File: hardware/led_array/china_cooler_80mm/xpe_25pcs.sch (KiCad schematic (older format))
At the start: 25 parts

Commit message: initial 80mm pcb draft ready
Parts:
- removed D10, D2, D3, D4, D5, D6, D7, D8, D9: royal blue, LEDs:LED-XP-G_CREE, symbol LED
- removed D11, D12, D13, D14, D15: blue, LEDs:LED-XP-G_CREE, symbol LED
- removed D16, D17, D18, D19, D20: white, LEDs:LED-XP-G_CREE, symbol LED
- removed D21, D22, D23, D24, D25: white_warm, LEDs:LED-XP-G_CREE, symbol LED
- added D1, D10, D2, D3, D4, D6, D7, D8, D9: royal blue, led:LED_Cree-XP-E, symbol led:LED
- added D11, D12, D13, D14, D15: blue, led:LED_Cree-XP-E, symbol led:LED
- added D16, D17, D18, D19, D20: white, led:LED_Cree-XP-E, symbol led:LED
- added D21, D22, D23, D24, D25: white_warm, led:LED_Cree-XP-E, symbol led:LED
- added J1: Conn_01x10, led:header_10_smd, symbol Connector_Generic:Conn_01x10
- D5: renamed from D1; footprint LEDs:LED-XP-G_CREE -> led:LED_Cree-XP-E; symbol LED -> led:LED
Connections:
- net GND: now also D5.1 (K), D10.1 (K), D15.1 (K), D20.1 (K), D25.1 (K), J1.10 (Pin_10), J1.6 (Pin_6), J1.7 (Pin_7), J1.8 (Pin_8), J1.9 (Pin_9)
- net at D5.2 (A): now also D4.1 (K)
- new net: D10.2 (A), D9.1 (K)
- new net: D3.1 (K), D4.2 (A)
- new net: D8.1 (K), D9.2 (A)
- new net: D2.1 (K), D3.2 (A)
- new net: D7.1 (K), D8.2 (A)
- new net: D1.1 (K), D2.2 (A)
- new net: D6.1 (K), D7.2 (A)
- new net: D1.2 (A), J1.5 (Pin_5)
- new net: D6.2 (A), J1.4 (Pin_4)
- new net: D14.1 (K), D15.2 (A)
- new net: D19.1 (K), D20.2 (A)
- new net: D21.2 (A), J1.1 (Pin_1)
- new net: D16.2 (A), J1.2 (Pin_2)
- new net: D11.2 (A), J1.3 (Pin_3)
- new net: D24.1 (K), D25.2 (A)
- new net: D13.1 (K), D14.2 (A)
- new net: D18.1 (K), D19.2 (A)
- new net: D23.1 (K), D24.2 (A)
- new net: D12.1 (K), D13.2 (A)
- new net: D17.1 (K), D18.2 (A)
- new net: D22.1 (K), D23.2 (A)
- new net: D11.1 (K), D12.2 (A)
- new net: D16.1 (K), D17.2 (A)
- new net: D21.1 (K), D22.2 (A)

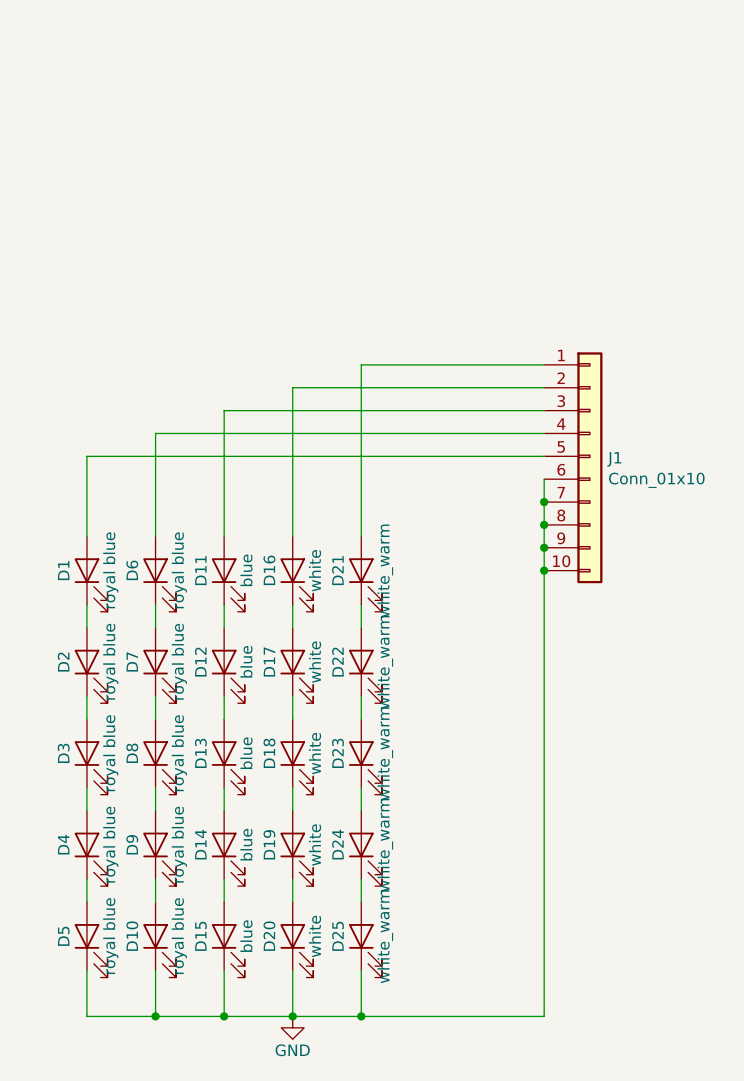
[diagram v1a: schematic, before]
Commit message: 25 led array improved
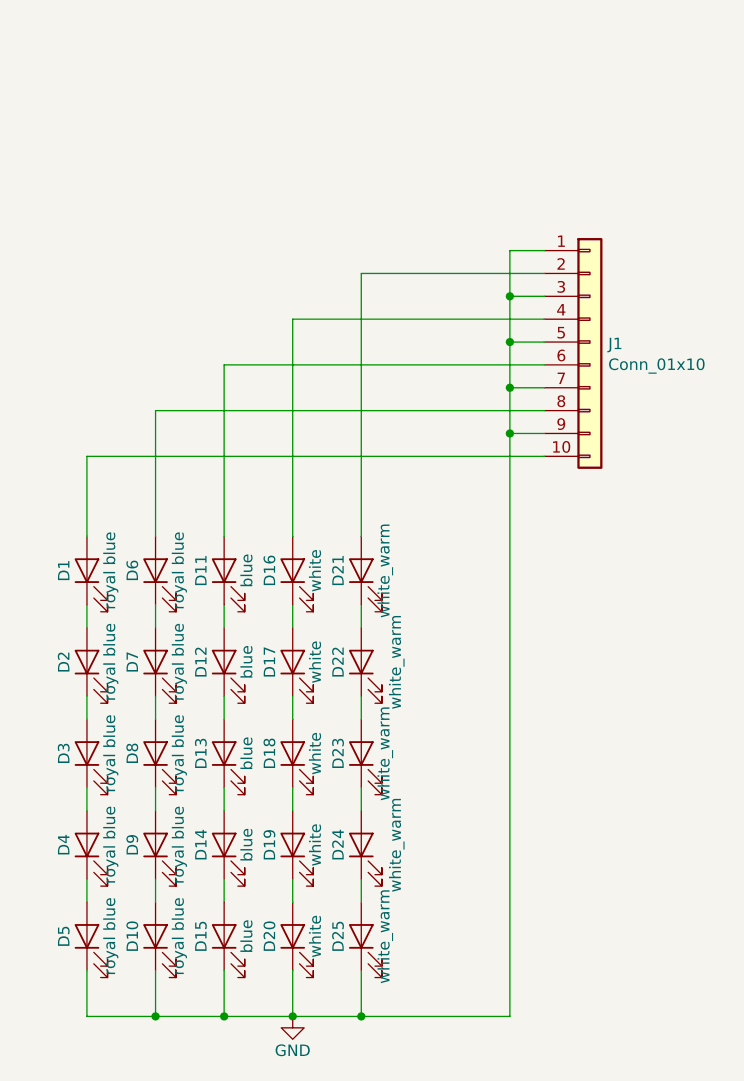
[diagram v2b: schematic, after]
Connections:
- net GND: now also J1.1 (Pin_1), J1.3 (Pin_3), J1.5 (Pin_5); no longer J1.10 (Pin_10), J1.6 (Pin_6), J1.8 (Pin_8)
- net at D1.2 (A): now also J1.10 (Pin_10); no longer J1.5 (Pin_5)
- net at D6.2 (A): now also J1.8 (Pin_8); no longer J1.4 (Pin_4)
- net at D21.2 (A): now also J1.2 (Pin_2); no longer J1.1 (Pin_1)
- net at D16.2 (A): now also J1.4 (Pin_4); no longer J1.2 (Pin_2)
- net at D11.2 (A): now also J1.6 (Pin_6); no longer J1.3 (Pin_3)
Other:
- moved on the sheet: J1
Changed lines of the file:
@@
 P 5400 4650
 F 0 "D24" H 5400 4750 50  0000 C CNN
-F 1 "white_warm" H 5400 4550 50  0000 C CNN
+F 1 "white_warm" H 5400 4500 50  0000 C CNN
 F 2 "led:LED_Cree-XP-E" H 5400 4650 50  0001 C CNN
 F 3 "" H 5400 4650 50  0000 C CNN
@@
 P 5400 3850
 F 0 "D22" H 5400 3950 50  0000 C CNN
-F 1 "white_warm" H 5400 3750 50  0000 C CNN
+F 1 "white_warm" H 5400 3700 50  0000 C CNN
 F 2 "led:LED_Cree-XP-E" H 5400 3850 50  0001 C CNN
 F 3 "" H 5400 3850 50  0000 C CNN
@@
 L Connector_Generic:Conn_01x10 J1
 U 1 1 5BF2DF76
-P 6400 2950
-F 0 "J1" H 6480 2942 50  0000 L CNN
-F 1 "Conn_01x10" H 6480 2851 50  0000 L CNN
-F 2 "led:header_10_smd" H 6400 2950 50  0001 C CNN
-F 3 "~" H 6400 2950 50  0001 C CNN
-	1    6400 2950
+P 6400 2450
+F 0 "J1" H 6480 2442 50  0000 L CNN
+F 1 "Conn_01x10" H 6480 2351 50  0000 L CNN
+F 2 "led:header_10_smd" H 6400 2450 50  0001 C CNN
+F 3 "~" H 6400 2450 50  0001 C CNN
+	1    6400 2450
 	1    0    0    -1
 $EndComp
-Wire Wire Line
-	6200 5400 5400 5400
-Wire Wire Line
-	6200 3050 6200 3150
-Connection ~ 6200 3150
-Wire Wire Line
-	6200 3150 6200 3250
-Connection ~ 6200 3250
-Wire Wire Line
-	6200 3250 6200 3350
-Connection ~ 6200 3350
-Wire Wire Line
-	6200 3350 6200 3450
-Connection ~ 6200 3450
-Wire Wire Line
-	6200 3450 6200 5400
 Connection ~ 5400 5400
-Wire Wire Line
-	6200 2750 4800 2750
-Wire Wire Line
-	6200 2650 5100 2650
-Wire Wire Line
-	6200 2550 5400 2550
 Wire Wire Line
 	4200 2950 4200 3300
 Wire Wire Line
-	4200 2950 6200 2950
+	6200 2850 6050 2850
 Wire Wire Line
-	4500 2850 4500 3300
+	6050 2650 6200 2650
 Wire Wire Line
-	4500 2850 6200 2850
+	6050 2650 6050 2450
 Wire Wire Line
-	4800 2750 4800 3300
+	6050 2450 6200 2450
+Connection ~ 6050 2650
 Wire Wire Line
-	5100 3300 5100 2650
+	6050 2450 6050 2250
 Wire Wire Line
-	5400 3300 5400 2550
+	6050 2250 6200 2250
+Connection ~ 6050 2450
+Wire Wire Line
+	6050 2250 6050 2050
+Wire Wire Line
+	6050 2050 6200 2050
+Connection ~ 6050 2250
+Wire Wire Line
+	5400 5400 6050 5400
+Connection ~ 6050 2850
+Wire Wire Line
+	6050 2650 6050 2850
+Wire Wire Line
+	6050 2850 6050 5400
+Wire Wire Line
+	6200 2950 4200 2950
+Wire Wire Line
+	4500 2750 4500 3300
+Wire Wire Line
+	4500 2750 6200 2750
+Wire Wire Line
+	5400 2150 6200 2150
+Wire Wire Line
+	5400 2150 5400 3300
+Wire Wire Line
+	5100 2350 5100 3300
+Wire Wire Line
+	5100 2350 6200 2350
+Wire Wire Line
+	6200 2550 4800 2550
+Wire Wire Line
+	4800 2550 4800 3300
 $EndSCHEMATC
